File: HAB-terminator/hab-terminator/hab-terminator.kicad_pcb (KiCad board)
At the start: 2 copper layers, 25 x 63.3 mm, 42 parts, among them J1 Battery, J2 Burn wire, J3 Actuator, J4 MSD-4-A, J5 Heater, Q1 DMN2053UVTQ-7, Q2 DMN2053UVTQ-7, Q3 AO3401A, Q4 AO3401A, SW2 SW_Push_EXT, U1 XIAO-ESP32-C3-SMD, U2 DRV8212P, U3 74LVC1G3157, U4 MS5607-02BA

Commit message: updating terminator
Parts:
- R14, R15: value 4.7k -> 10k
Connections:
- Q3 pad 2: +BATT -> /VBAT
- Q3 pad 3: /VBAT -> +BATT
- Q4 pad 2: GND -> Net-(J5-Pin_2)
- Q4 pad 3: Net-(J5-Pin_2) -> GND
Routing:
- net +BATT: track 87.7 -> 47.2 mm
- net +3V3: track 84.9 -> 51.8 mm
- net /BURN_EN/ACT_1: track 33.2 -> 13.0 mm
- net /SW_SNS/ACT_2: track 34.9 -> 15.5 mm
- net /BURN_ARM/PWR_HOLD: track 53.0 -> 36.4 mm
- net /HEATER_EN/A_MUX: track 47.1 -> 31.1 mm
- net /NTC/VBAT_SNS: track 23.5 -> 8.98 mm
- net /I2C_SDA: track 10.6 -> 0.00 mm
- net Net-(Q2B-G): track 10.3 -> 0.00 mm
- net /CSB/~{SLEEP}: track 9.33 -> 0.00 mm
- net Net-(Q2A-D): track 8.93 -> 0.00 mm
- net /I2C_SCL: track 15.1 -> 7.48 mm
- net /VBAT: track 17.9 -> 10.5 mm
- net Net-(R20-Pad2): track 7.15 -> 0.00 mm
- net /SD_CS: track 30.2 -> 23.8 mm
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- added copper zone on In1.Cu, net +3V3
- added copper zone on In2.Cu, net GND
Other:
- copper layers 2 -> 4

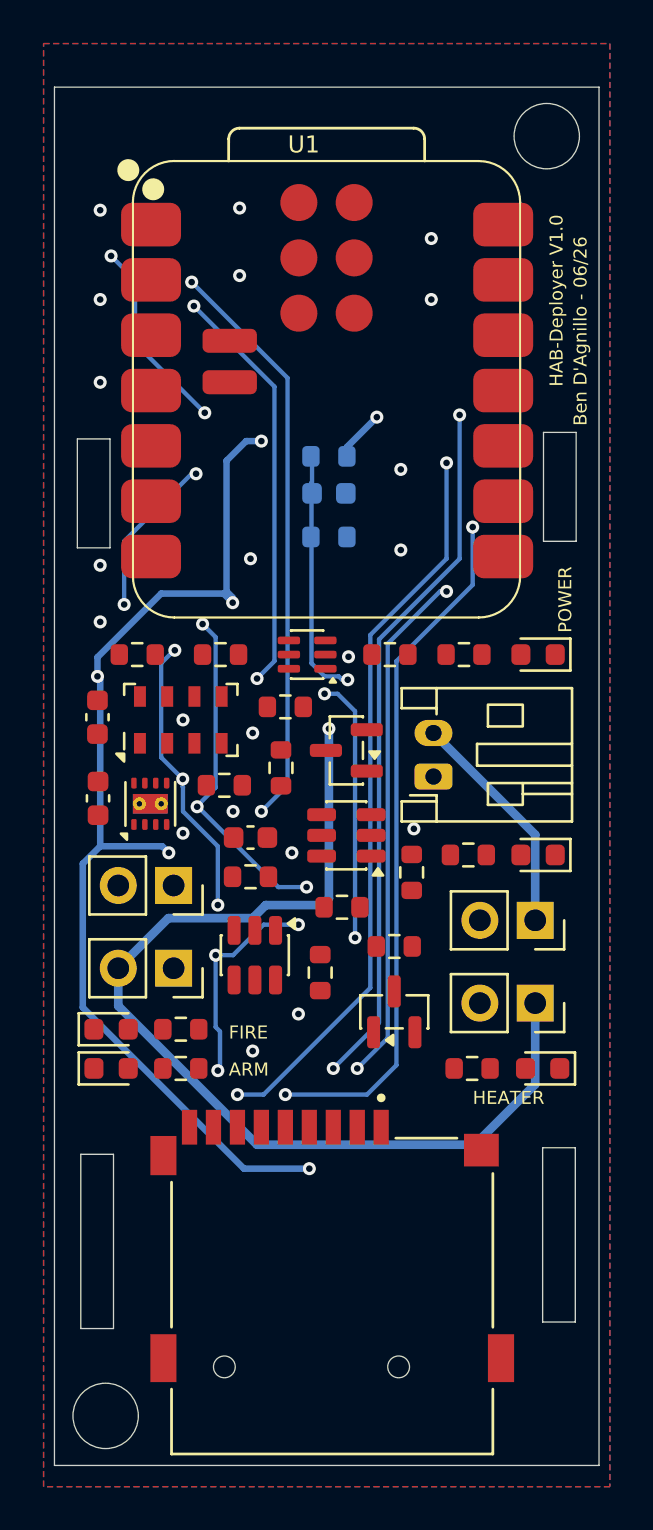
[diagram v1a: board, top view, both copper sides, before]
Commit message: updated terminator layout
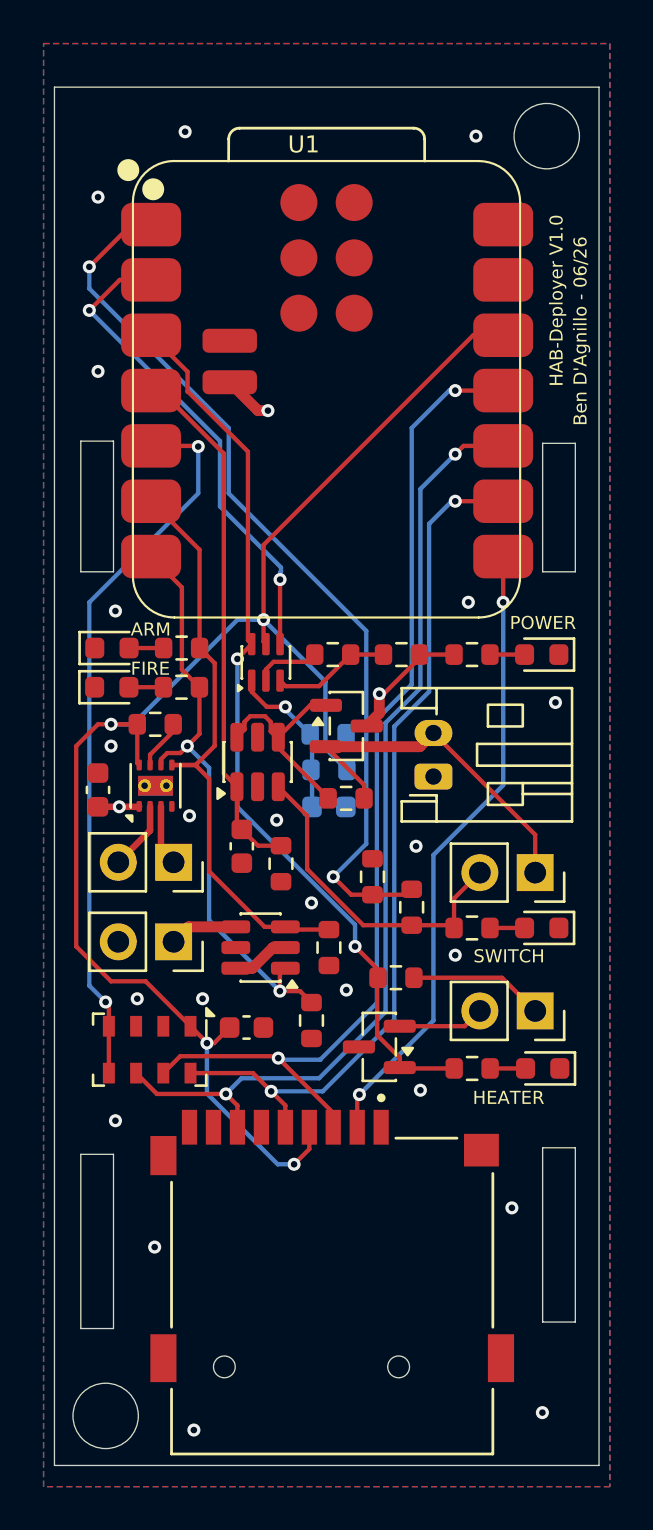
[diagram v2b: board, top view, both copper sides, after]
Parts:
- removed R15: 10k, Resistor_SMD:R_0603_1608Metric
- R11, R14, R18: value 10k -> 100k
- R20, R21: value 150k -> 100k
- moved G*** 46.8 mm to (96.9, 103.0)
- moved D2 19.3 mm to (87.0, 120.5)
- moved R4 19.3 mm to (90.2, 120.5)
- moved C6 15.8 mm to (93.2, 137.9), turned to 0 degrees
- moved D1 15.7 mm to (87.0, 122.3)
- moved R3 15.7 mm to (90.2, 122.3)
- moved U4 15.2 mm to (88.8, 138.9), turned to -90 degrees
- moved C2 14.4 mm to (97.0, 127.8)
- moved R9 14.4 mm to (97.0, 126.1)
- moved R14 14.3 mm to (97.0, 134.2), turned to -90 degrees
- moved TH1 9.06 mm to (97.0, 124.5)
- moved Q2 5.29 mm to (93.7, 125.7), turned to 90 degrees
- moved R10 4.23 mm to (89.0, 124.0)
- moved D3 3.35 mm to (106.8, 133.3)
- moved R16 3.35 mm to (103.6, 133.3)
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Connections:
- C4 pad 1: +BATT -> GND
- C7 pad 2: /BURN_ARM/PWR_HOLD -> /PWR_HOLD
- J5 pad 1: +BATT -> GND
- Q1 pad 3: /BURN_ARM/PWR_HOLD -> /BURN_ARM/ACT_2
- Q2 pad 1: /BURN_ARM/PWR_HOLD -> /PWR_HOLD
- Q3 pad 3: +BATT -> GND
- R10 pad 1: /CSB/~{SLEEP} -> Net-(U2-~{SLEEP})
- R11 pad 1: /SW_SNS/ACT_2 -> /SW_SNS
- R12 pad 2: /BURN_ARM/PWR_HOLD -> /PWR_HOLD
- R14 pad 1: /I2C_SDA -> /BURN_ARM/ACT_2
- R14 pad 2: +3V3 -> GND
- R17 pad 1: +BATT -> GND
- R18 pad 2: /SW_SNS/ACT_2 -> /SW_SNS
- R19 pad 2: +BATT -> GND
- R21 pad 1: +BATT -> GND
- R4 pad 2: /BURN_ARM/PWR_HOLD -> /BURN_ARM/ACT_2
- U1 pad 1: /NTC/VBAT_SNS -> /SW_SNS
- U1 pad 2: /BURN_ARM/PWR_HOLD -> /NTC/VBAT_SNS
- U1 pad 21: +BATT -> GND
- U1 pad 4: /SW_SNS/ACT_2 -> /PWR_HOLD
- U1 pad 5: /I2C_SCL -> /MS5607_CS
- U1 pad 6: /I2C_SDA -> /BURN_ARM/ACT_2
- U2 pad 1: +BATT -> GND
- U2 pad 5: /SW_SNS/ACT_2 -> /BURN_ARM/ACT_2
- U2 pad 7: /CSB/~{SLEEP} -> Net-(U2-~{SLEEP})
- U4 pad 2: +3V3 -> GND
- U4 pad 4: /CSB/~{SLEEP} -> /MS5607_CS
- U4 pad 5: /CSB/~{SLEEP} -> /MS5607_CS
- U4 pad 6: unconnected-(U4-SDO-Pad6) -> /SPI_MISO
- U4 pad 7: /I2C_SDA -> /SPI_MOSI
- U4 pad 8: /I2C_SCL -> /SPI_CLK
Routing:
- net +BATT: track 47.2 -> 0.00 mm, vias 1 -> 0
- net /SW_SNS: track 0.00 -> 41.6 mm, vias 0 -> 2
- net /BURN_ARM/PWR_HOLD: track 36.4 -> 0.00 mm, vias 5 -> 0
- net /MS5607_CS: track 0.00 -> 33.4 mm, vias 0 -> 2
- net /BURN_ARM/ACT_2: track 0.00 -> 27.6 mm
- net /PWR_HOLD: track 0.00 -> 24.5 mm
- net GND: track 0.07 -> 19.4 mm, vias 21 -> 25
- net +3V3: track 51.8 -> 70.1 mm, vias 6 -> 4
- net /SW_SNS/ACT_2: track 15.5 -> 0.00 mm, vias 3 -> 0
- net Net-(Q2B-G): track 0.00 -> 15.2 mm
- net /SPI_MOSI: track 32.4 -> 47.5 mm
- net /BURN_EN/ACT_1: track 13.0 -> 27.4 mm, vias 3 -> 2
- net /NTC/VBAT_SNS: track 8.98 -> 22.4 mm
- net /SPI_MISO: track 33.7 -> 44.4 mm
- net /HEATER_EN/A_MUX: track 31.1 -> 41.4 mm, vias 4 -> 2
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- added copper zone on In1.Cu, net +BATT
- removed copper zone on In1.Cu, net +3V3
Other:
- outline, holes or cut-outs redrawn
- board text added: "SWITCH"
